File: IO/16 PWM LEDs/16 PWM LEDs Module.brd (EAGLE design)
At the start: 25.4 x 25.4 mm, 24 parts, among them U1 PCA9685

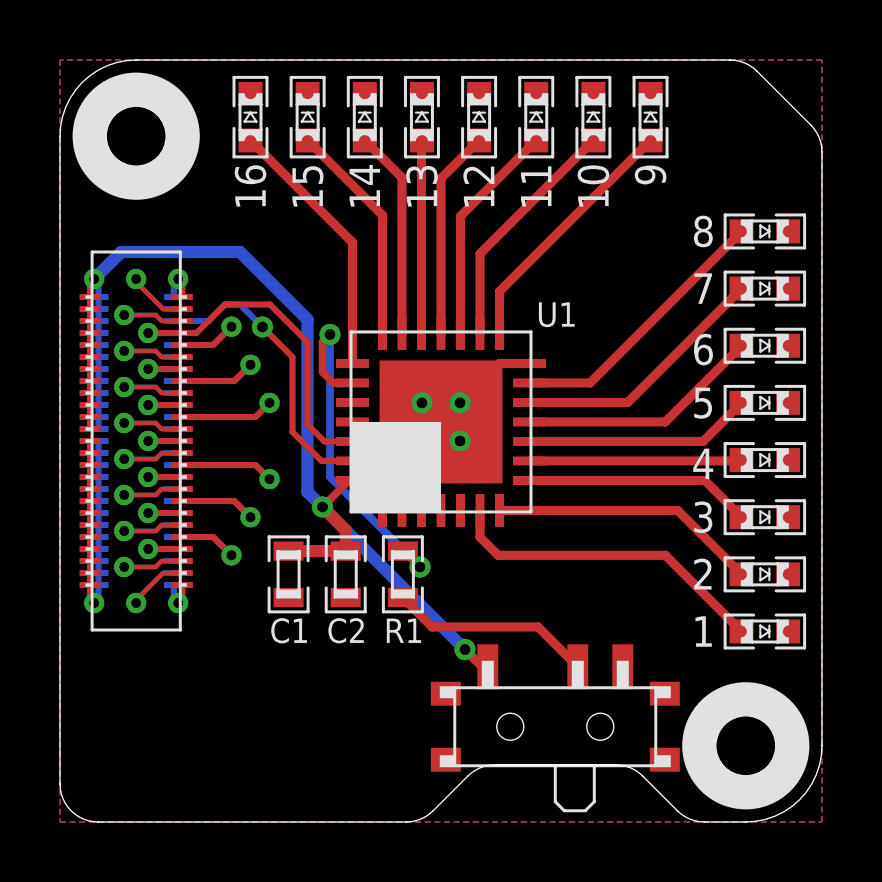
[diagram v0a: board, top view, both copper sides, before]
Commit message: 16 PWM LEDs Module: -Change package of C2
Signed-off-by: Cruz Monrreal II <Cruz.Monrreal@gmail.com>
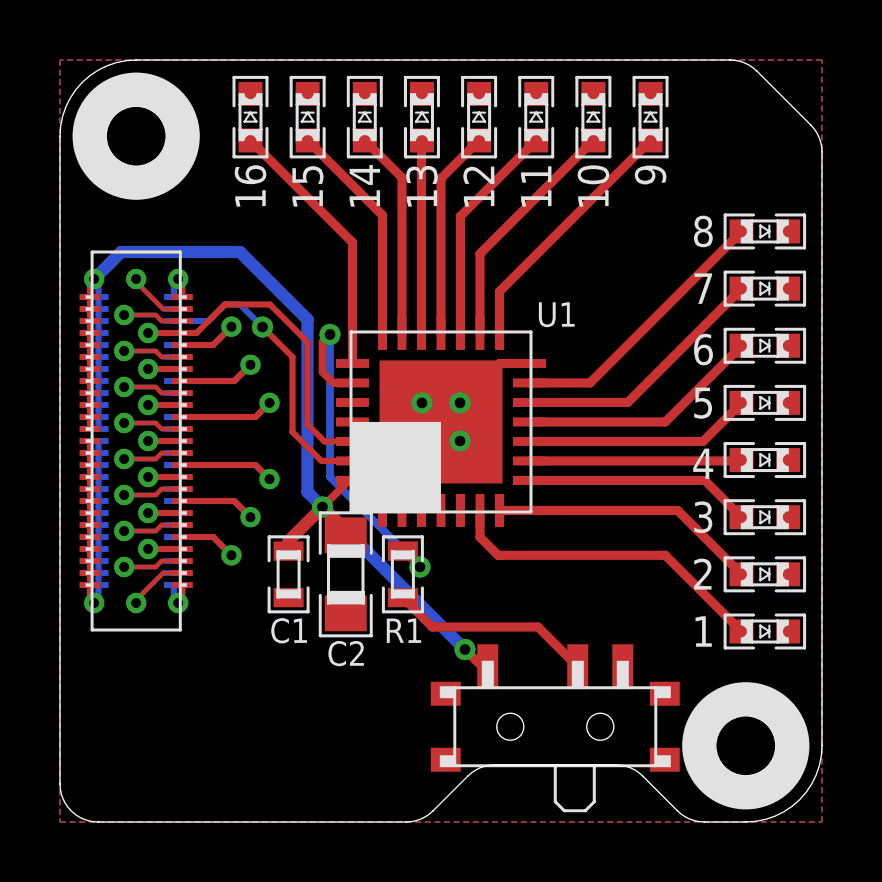
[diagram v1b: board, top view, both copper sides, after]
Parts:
- C2: device .standardparts:0603 -> .standardparts:0805
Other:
- board text added: "v1.1"
- board text removed: "v1"
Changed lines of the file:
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@@
 <text x="12.7" y="5.715" size="1.016" layer="52" font="vector" ratio="12" rot="MR0" align="bottom-center">Cruz Monrreal II</text>
 <text x="12.7" y="4.445" size="1.016" layer="52" font="vector" ratio="12" rot="MR0" align="bottom-center">InnovativeMaker.com</text>
-<text x="0.635" y="1.27" size="1.016" layer="52" font="vector" ratio="12" rot="MR0" align="bottom-right">v1</text>
+<text x="0.635" y="1.27" size="1.016" layer="52" font="vector" ratio="12" rot="MR0" align="bottom-right">v1.1</text>
 </plain>
 <attributes>
@@
 <attribute name="NAME" x="6.985" y="5.969" size="0.8128" layer="25" font="vector" ratio="12"/>
 </element>
-<element name="C2" library=".standardparts" package="0603" value="10uF" x="9.525" y="8.255" smashed="yes" rot="R270">
-<attribute name="NAME" x="8.89" y="5.969" size="0.8128" layer="25" font="vector" ratio="12"/>
+<element name="C2" library=".standardparts" package="0805" value="10uF" x="9.525" y="8.255" smashed="yes" rot="R270">
+<attribute name="NAME" x="8.89" y="5.207" size="0.8128" layer="25" font="vector" ratio="12"/>
 </element>
 <element name="U$11" library="alps" package="SSSS810701" value="SSSS810701" x="16.51" y="3.175" smashed="yes">
@@
 <wire x1="6" y1="19" x2="2.04" y2="19" width="0.4064" layer="16"/>
 <wire x1="2.04" y1="19" x2="1.14" y2="18.1" width="0.4064" layer="16"/>
-<wire x1="9.525" y1="9.725" x2="8.75" y2="10.5" width="0.4064" layer="1"/>
-<wire x1="9.525" y1="9.725" x2="9.525" y2="9.03" width="0.4064" layer="1"/>
-<wire x1="7.62" y1="9.03" x2="9.525" y2="9.03" width="0.4064" layer="1"/>
+<wire x1="9.525" y1="9.725" x2="9.525" y2="9.555" width="0.4064" layer="1"/>
 <wire x1="8.75" y1="10.5" x2="13.5" y2="5.75" width="0.4064" layer="16"/>
 <wire x1="9.75" y1="11.385" x2="9.635" y2="11.385" width="0.254" layer="1"/>
@@
 <wire x1="13.5" y1="5.75" x2="14.075" y2="5.175" width="0.3048" layer="1"/>
 <wire x1="14.075" y1="5.175" x2="14.26" y2="5.175" width="0.3048" layer="1"/>
+<wire x1="7.62" y1="9.03" x2="7.62" y2="9.37" width="0.4064" layer="1"/>
+<wire x1="7.62" y1="9.37" x2="8.75" y2="10.5" width="0.4064" layer="1"/>
+<wire x1="9.525" y1="9.725" x2="8.75" y2="10.5" width="0.4064" layer="1"/>
 </signal>
 <signal name="N$1">
